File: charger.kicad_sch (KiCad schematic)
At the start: 37 parts, among them Q1 NMOS, Q2 NMOS, Q3 NMOS, SW3 SW_SPST, U2 BQ25798RQMR

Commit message: added todos
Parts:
- added D3: D_Schottky, symbol Device:D_Schottky
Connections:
- net SYS+: now also D3.1 (K)
- net at R5.2, U2.18 (BATP): now also D3.2 (A)
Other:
- note added: "todo: find viable diode"
- note added: "todo: how to enable ship mode?"
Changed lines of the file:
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@@
 		)
 	)
+	(text "todo: find viable diode"
+		(exclude_from_sim no)
+		(at 226.314 80.01 0)
+		(effects
+			(font
+				(size 1.27 1.27)
+			)
+		)
+	)
+	(text "todo: how to enable ship mode?"
+		(exclude_from_sim no)
+		(at 226.314 102.108 0)
+		(effects
+			(font
+				(size 1.27 1.27)
+			)
+		)
+	)
 	(text_box "ILIM_HIZ pulled to REGN to set the Charging Current Lmit to max. Register Value limits it to 1A by default anyways"
 		(exclude_from_sim no)
@@
 		)
 	)
-	(text_box "@ToDO: Calculate correct resistor values. These are for the 103AT-2, while the LCSC points to a similar but not the same one\nFor AT103-2 these values equate to T_low = 0°C and T_high = 60°C\n"
+	(text_box "@ToDO: Calculate correct resistor values. These are for the 103AT-2, while the LCSC points to a similar but not the same one\nFor AT103-2 these values equate to T_low = 0°C and T_high = 60°C\n\nfind viable SMD thermistor"
 		(exclude_from_sim no)
 		(at 205.74 125.73 0)
-		(size 41.91 13.97)
+		(size 41.91 17.78)
 		(margins 0.9525 0.9525 0.9525 0.9525)
 		(stroke
@@
 	)
 	(junction
+		(at 208.28 72.39)
+		(diameter 0)
+		(color 0 0 0 0)
+	)
+	(junction
 		(at 111.76 41.91)
 		(diameter 0)
@@
 	)
 	(junction
+		(at 208.28 88.9)
+		(diameter 0)
+		(color 0 0 0 0)
+	)
+	(junction
 		(at 168.91 41.91)
 		(diameter 0)
@@
 	(wire
 		(pts
+			(xy 208.28 72.39) (xy 208.28 77.47)
+		)
+		(stroke
+			(width 0)
+			(type default)
+		)
+	)
+	(wire
+		(pts
 			(xy 204.47 100.33) (xy 201.93 100.33)
 		)
@@
 	(wire
 		(pts
-			(xy 166.37 88.9) (xy 209.55 88.9)
+			(xy 166.37 88.9) (xy 208.28 88.9)
 		)
 		(stroke
@@
 	(wire
 		(pts
+			(xy 208.28 88.9) (xy 209.55 88.9)
+		)
+		(stroke
+			(width 0)
+			(type default)
+		)
+	)
+	(wire
+		(pts
 			(xy 158.75 49.53) (xy 168.91 49.53)
 		)
@@
 	(wire
 		(pts
+			(xy 208.28 72.39) (xy 199.39 72.39)
+		)
+		(stroke
+			(width 0)
+			(type default)
+		)
+	)
+	(wire
+		(pts
 			(xy 83.82 72.39) (xy 88.9 72.39)
 		)
@@
 	(wire
 		(pts
+			(xy 208.28 85.09) (xy 208.28 88.9)
+		)
+		(stroke
+			(width 0)
+			(type default)
+		)
+	)
+	(wire
+		(pts
 			(xy 168.91 41.91) (xy 175.26 41.91)
 		)
@@
 	(wire
 		(pts
-			(xy 208.28 72.39) (xy 199.39 72.39)
+			(xy 210.82 72.39) (xy 208.28 72.39)
 		)
 		(stroke
@@
 	(hierarchical_label "SYS+"
 		(shape input)
-		(at 208.28 72.39 0)
+		(at 210.82 72.39 0)
 		(effects
 			(font
@@
 					(unit 1)
 				)
+			)
+		)
+	)
+	(symbol
+		(lib_id "Device:D_Schottky")
+		(at 208.28 81.28 270)
+		(unit 1)
+		(exclude_from_sim no)
+		(in_bom yes)
+		(on_board yes)
+		(dnp no)
+		(fields_autoplaced yes)
+		(property "Reference" "D3"
+			(at 210.82 79.6924 90)
+			(effects
+				(font
+					(size 1.27 1.27)
+				)
+				(justify left)
+			)
+		)
+		(property "Value" "D_Schottky"
+			(at 210.82 82.2324 90)
+			(effects
+				(font
+					(size 1.27 1.27)
+				)
+				(justify left)
+			)
+		)
+		(property "Footprint" ""
+			(at 208.28 81.28 0)
+			(effects
+				(font
+					(size 1.27 1.27)
+				)
+				(hide yes)
+			)
+		)
+		(property "Datasheet" "~"
+			(at 208.28 81.28 0)
+			(effects
+				(font
+					(size 1.27 1.27)
+				)
+				(hide yes)
+			)
+		)
+		(property "Description" "Schottky diode"
+			(at 208.28 81.28 0)
+			(effects
+				(font
+					(size 1.27 1.27)
+				)
+				(hide yes)
+			)
+		)
+		(pin "1"
+		)
+		(pin "2"
+		)
+		(instances
+			(project ""
+				(path "/afc8cbd3-9ea8-40a2-afae-ed6bd0fe7e6e/29a18ff5-2f4c-44c0-998a-9c2a7b324824"
+					(reference "D3")
+					(unit 1)
+				)

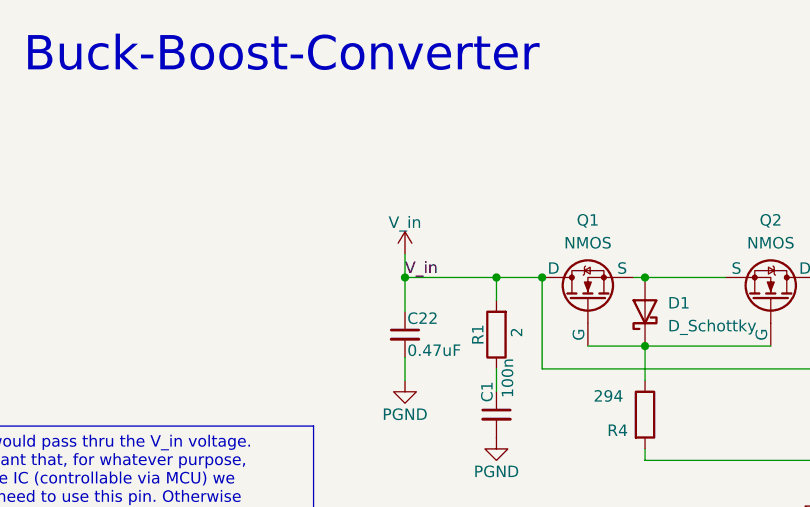
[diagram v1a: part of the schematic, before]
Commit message: added hierarchical pins for submodules
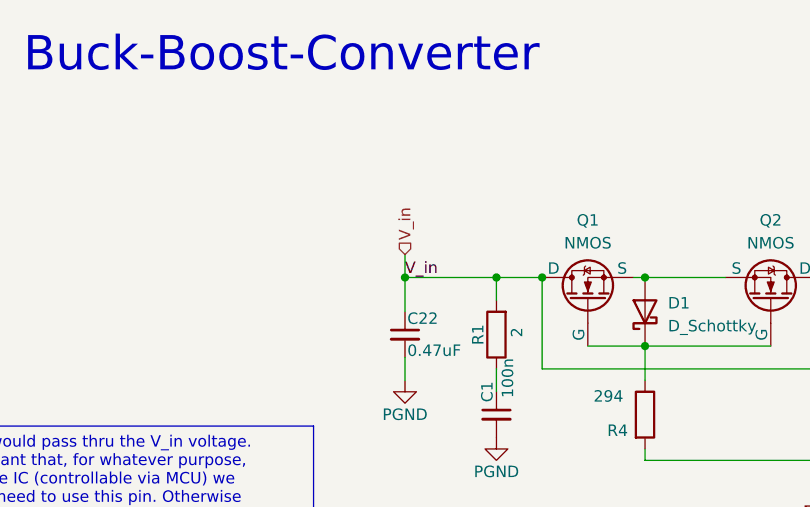
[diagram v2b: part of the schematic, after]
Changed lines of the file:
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@@
 		)
 	)
+	(hierarchical_label "V_in"
+		(shape input)
+		(at 66.04 39.37 90)
+		(effects
+			(font
+				(size 1.27 1.27)
+			)
+			(justify left)
+		)
+	)
 	(hierarchical_label "CE_N"
 		(shape input)
@@
 					(unit 1)
 				)
-			)
-		)
-	)
-	(symbol
-		(lib_name "VDC_1")
-		(lib_id "power:VDC")
-		(at 66.04 39.37 0)
-		(unit 1)
-		(exclude_from_sim no)
-		(in_bom yes)
-		(on_board yes)
-		(dnp no)
-		(property "Reference" "#PWR035"
-			(at 66.04 43.18 0)
-			(effects
-				(font
-					(size 1.27 1.27)
-				)
-				(hide yes)
-			)
-		)
-		(property "Value" "V_in"
-			(at 66.04 35.814 0)
-			(effects
-				(font
-					(size 1.27 1.27)
-				)
-			)
-		)
-		(property "Footprint" ""
-			(at 66.04 39.37 0)
-			(effects
-				(font
-					(size 1.27 1.27)
-				)
-				(hide yes)
-			)
-		)
-		(property "Datasheet" ""
-			(at 66.04 39.37 0)
-			(effects
-				(font
-					(size 1.27 1.27)
-				)
-				(hide yes)
-			)
-		)
-		(property "Description" "Power symbol creates a global label with name \"VDC\""
-			(at 66.04 39.37 0)
-			(effects
-				(font
-					(size 1.27 1.27)
-				)
-				(hide yes)
-			)
-		)
-		(pin "1"
-		)
-		(instances
-			(project "rapid_power_module"
-				(path "/afc8cbd3-9ea8-40a2-afae-ed6bd0fe7e6e/29a18ff5-2f4c-44c0-998a-9c2a7b324824"
-					(reference "#PWR035")
-					(unit 1)
-				)

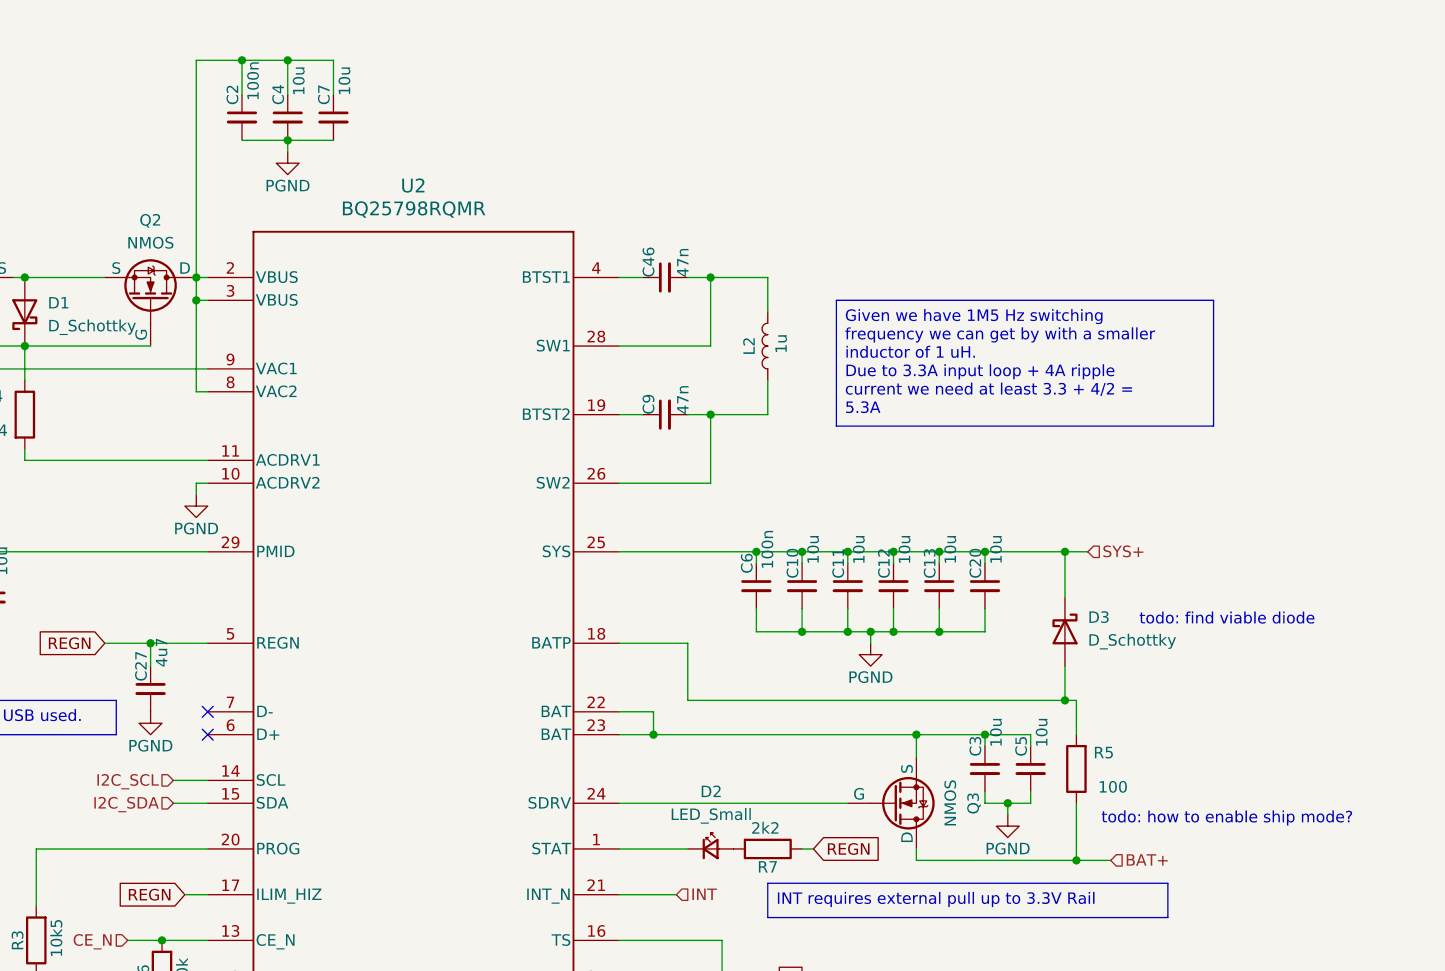
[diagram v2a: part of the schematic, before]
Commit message: added second i2c bus; cleaned up sub-schematic-structure
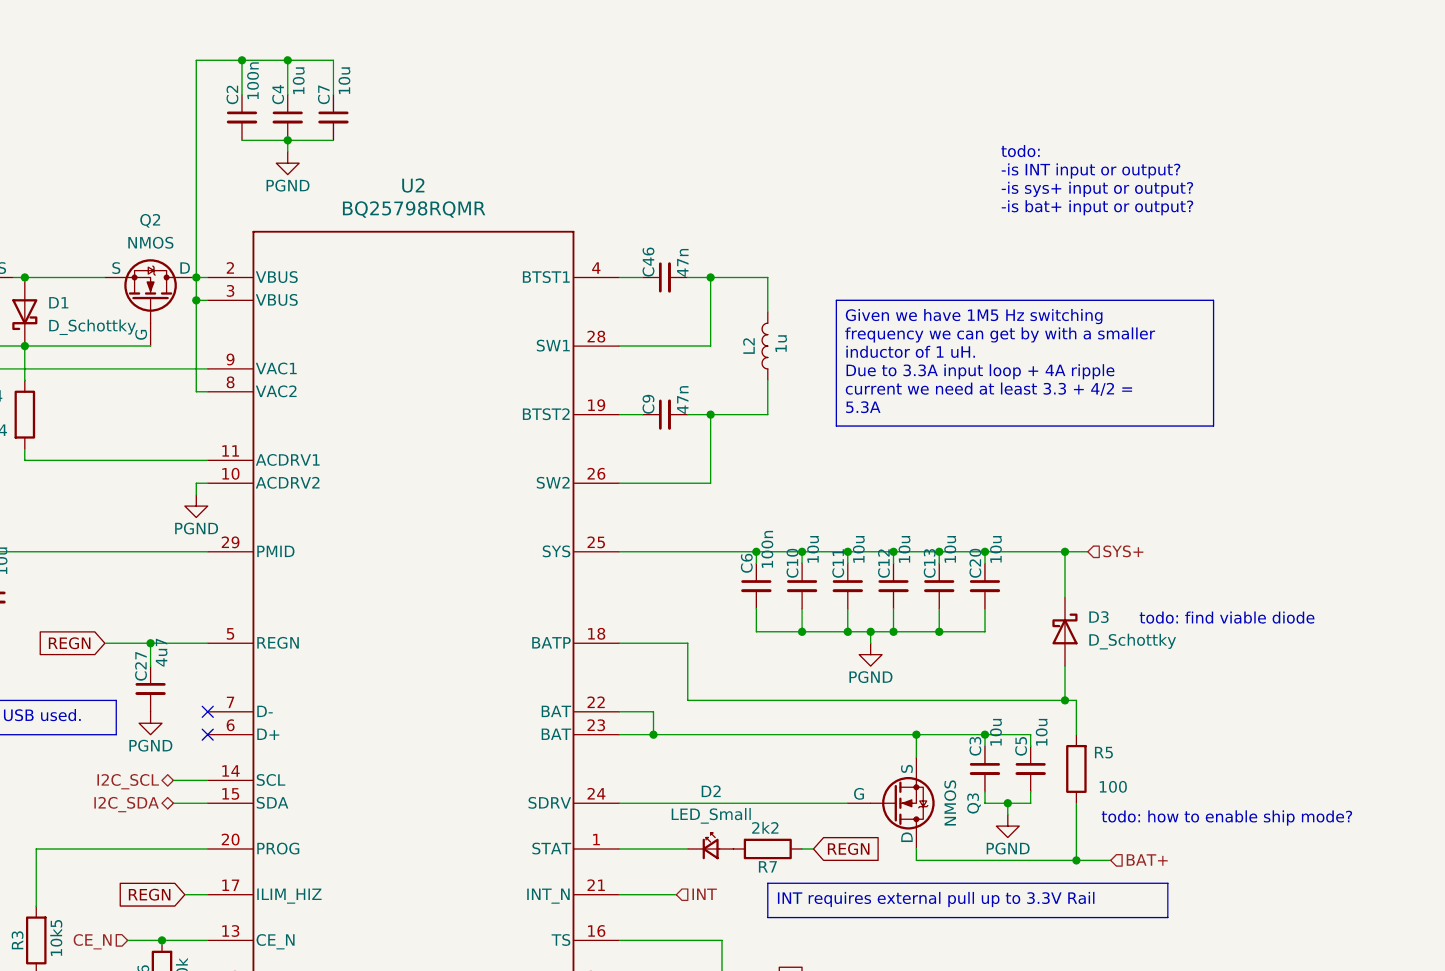
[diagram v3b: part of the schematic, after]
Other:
- note added: "todo: -is INT input or output? -is sys+ input or output? -is bat+ input or output?"
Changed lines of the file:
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@@
+		)
+	)
+	(text "todo: \n-is INT input or output?\n-is sys+ input or output?\n-is bat+ input or output?"
+		(exclude_from_sim no)
+		(at 201.168 31.242 0)
+		(effects
+			(font
+				(size 1.27 1.27)
+			)
+			(justify left)
 		)
 	)
@@
 	)
 	(hierarchical_label "I2C_SDA"
-		(shape input)
+		(shape bidirectional)
 		(at 109.22 100.33 180)
 		(effects
@@
 	)
 	(hierarchical_label "I2C_SCL"
-		(shape input)
+		(shape bidirectional)
 		(at 109.22 97.79 180)
 		(effects

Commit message: Cleaned up, added some Balancer designs
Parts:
- added D12: ~, Diode_SMD:D_SMA, symbol Device:D_Schottky
- TH1: footprint Resistor_THT:R_Axial_DIN0204_L3.6mm_D1.6mm_P2.54mm_Vertical -> Capacitor_SMD:C_0201_0603Metric; LCSC C3000142 -> C2889048
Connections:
- net V_in: now also D12.1 (K), D12.2 (A)
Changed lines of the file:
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@@
 		)
 	)
-	(text_box "@ToDO: Calculate correct resistor values. These are for the 103AT-2, while the LCSC points to a similar but not the same one\nFor AT103-2 these values equate to T_low = 0°C and T_high = 60°C\n\nfind viable SMD thermistor"
+	(text_box "@ToDO: Calculate correct resistor values. These are for the 103AT-2, while the LCSC points to a similar but not the same one\nFor AT103-2 these values equate to T_low = 0°C and T_high = 60°C\n\nfind viable SMD thermistor: Done; C2889048"
 		(exclude_from_sim no)
 		(at 205.74 125.73 0)
-		(size 41.91 17.78)
+		(size 46.99 17.78)
 		(margins 0.9525 0.9525 0.9525 0.9525)
 		(stroke
@@
 	)
 	(junction
-		(at 168.91 57.15)
+		(at 66.04 41.91)
 		(diameter 0)
 		(color 0 0 0 0)
 	)
 	(junction
-		(at 66.04 41.91)
+		(at 168.91 57.15)
 		(diameter 0)
 		(color 0 0 0 0)
@@
 	(wire
 		(pts
-			(xy 66.04 39.37) (xy 66.04 41.91)
-		)
-		(stroke
-			(width 0)
-			(type default)
-		)
-	)
-	(wire
-		(pts
 			(xy 73.66 80.01) (xy 73.66 81.28)
 		)
@@
 	(wire
 		(pts
+			(xy 66.04 26.67) (xy 66.04 30.48)
+		)
+		(stroke
+			(width 0)
+			(type default)
+		)
+	)
+	(wire
+		(pts
 			(xy 194.31 78.74) (xy 194.31 81.28)
 		)
@@
 	(wire
 		(pts
+			(xy 66.04 38.1) (xy 66.04 41.91)
+		)
+		(stroke
+			(width 0)
+			(type default)
+		)
+	)
+	(wire
+		(pts
 			(xy 83.82 81.28) (xy 81.28 81.28)
 		)
@@
 	(hierarchical_label "V_in"
 		(shape input)
-		(at 66.04 39.37 90)
+		(at 66.04 26.67 90)
 		(effects
 			(font
@@
 			)
 		)
-		(property "Footprint" "Resistor_THT:R_Axial_DIN0204_L3.6mm_D1.6mm_P2.54mm_Vertical"
+		(property "Footprint" "Capacitor_SMD:C_0201_0603Metric"
 			(at 190.5 135.89 0)
 			(effects
@@
 			)
 		)
-		(property "LCSC" "C3000142"
+		(property "LCSC" "C2889048"
 			(at 191.77 135.89 90)
 			(effects
@@
 					(unit 1)
 				)
+			)
+		)
+	)
+	(symbol
+		(lib_id "Device:D_Schottky")
+		(at 66.04 34.29 90)
+		(unit 1)
+		(exclude_from_sim no)
+		(in_bom yes)
+		(on_board yes)
+		(dnp no)
+		(property "Reference" "D12"
+			(at 68.834 34.544 0)
+			(effects
+				(font
+					(size 1.27 1.27)
+				)
+			)
+		)
+		(property "Value" "~"
+			(at 69.85 34.6075 0)
+			(effects
+				(font
+					(size 1.27 1.27)
+				)
+				(hide yes)
+			)
+		)
+		(property "Footprint" "Diode_SMD:D_SMA"
+			(at 66.04 34.29 0)
+			(effects
+				(font
+					(size 1.27 1.27)
+				)
+				(hide yes)
+			)
+		)
+		(property "Datasheet" "https://www.lcsc.com/datasheet/C22452.pdf"
+			(at 66.04 34.29 0)
+			(effects
+				(font
+					(size 1.27 1.27)
+				)
+				(hide yes)
+			)
+		)
+		(property "Description" "Schottky diode"
+			(at 66.04 34.29 0)
+			(effects
+				(font
+					(size 1.27 1.27)
+				)
+				(hide yes)
+			)
+		)
+		(property "LCSC" "C22452"
+			(at 66.04 34.29 0)
+			(effects
+				(font
+					(size 1.27 1.27)
+				)
+				(hide yes)
+			)
+		)
+		(pin "2"
+		)
+		(pin "1"
+		)
+		(instances
+			(project "rapid_power_module"
+				(path "/afc8cbd3-9ea8-40a2-afae-ed6bd0fe7e6e/29a18ff5-2f4c-44c0-998a-9c2a7b324824"
+					(reference "D12")
+					(unit 1)
+				)
